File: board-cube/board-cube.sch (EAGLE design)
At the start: 95 parts, among them U1 TPS79933QDDCRQ1, U2 TPS79933QDDCRQ1, X1 SMA-142-0711-821/826, X10 SMA-142-0711-821/826, X2 SMA-142-0711-821/826, X3 SMA-142-0711-821/826, X4 SMA-142-0711-821/826, X5 SMA-142-0711-821/826, X6 SMA-142-0711-821/826, X7 SMA-142-0711-821/826, X8 SMA-142-0711-821/826, X9 SMA-142-0711-821/826

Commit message: more work
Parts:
- removed SV1, SV2: (no value), con-lstb:MA08-1
- added C4, C56: 100n, passives-7351:CAPACITOR0603-N
- added C57, C58: 1u, passives-7351:CAPACITOR0603-N
- added C59: 470n, passives-7351:CAPACITOR0603-N
- added C60: (no value), passives-7351:CAPACITOR0603-N
- added IC1: MSP430FR5739DA, Mine:MSP430FR5739DA
- added J1: TM4_SHIELD, cube-parts:TM4_SHIELD
- added JP10, JP9: (no value), SparkFun-Connectors:M03X22X3_SILK_MALE_PTH
- added JP5: FTDI_BASICPTH, SparkFun-Connectors:FTDI_BASICPTH
- added JP6: (no value), SparkFun-Connectors:M04PTH
- added LED1, LED2, LED3, LED4, LED5, LED6, LED7: (no value), dtb:LEDCHIP-LED0603
- added Q1: BSS84, transistor-small-signal:BSS84
- added R10, R11, R12, R13, R14, R8, R9: (no value), passives-7351:RESISTOR0603-N
- added R6, R7: 100k, passives-7351:RESISTOR0603-N
- added TP1, TP2, TP3: PTR1PAD1-20, testpad:PTR1PAD1-20
- R4: value 10k -> 100k
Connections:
- removed net N$43: SV2.2, U$4.CSN
- removed net N$44: SV2.1, U$4.NRESET
- removed net N$58: R4.P$1, U1.EN
- new net +3V3: C4.1, C56.1, C57.1, C58.1, IC1.AVCC, IC1.DVCC, J1.3V3, JP5.4
- new net A0_CLK: IC1.P1.5, JP9.3
- new net A0_CS: IC1.P1.4, JP9.1
- new net A0_SIMO: IC1.P2.0, JP9.5
- new net A1_RX: IC1.P2.6, J1.PB1, JP5.3
- new net A1_TX: IC1.P2.5, J1.PB0, JP5.2
- new net B0_CLK: IC1.P2.2, JP10.3
- new net B0_CS: IC1.P1.3, JP10.1
- new net B0_SIMO: IC1.P1.6, JP10.5
- new net INT_IN: IC1.P1.1, J1.PD7
- new net INT_OUT: IC1.P1.2, J1.PF4
- new net N$6: JP2.2, Q1.D
- new net RST: IC1.!RST, J1.RST
- new net RST_MAINBRD: IC1.P1.0, J1.PD6
- new net RX_CLK: J1.PA7, JP10.4, U$4.SCK
- new net RX_CS: J1.PA4, JP10.2, U$4.CSN
- new net RX_GPIO0: IC1.P3.5, J1.PC4, TP3.TP, U$4.GPIO0
- new net RX_GPIO2: IC1.P3.6, J1.PC5, U$4.GPIO2
- new net RX_GPIO3: IC1.P3.7, J1.PC6, U$4.GPIO3
- new net RX_MISO: IC1.P1.7, J1.PA6, U$4.MISO
- new net RX_MOSI: J1.PA5, JP10.6, U$4.MOSI
- new net RX_RST: IC1.P3.1, J1.PA2, R7.P$1, U$4.NRESET
- new net TX_CLK: J1.PB4, JP9.4, U$1.SCK
- new net TX_CS: J1.PE0, JP9.2, U$1.CSN
- new net TX_GPIO0: IC1.P3.2, J1.PF2, TP2.TP, U$1.GPIO0
- new net TX_GPIO2: IC1.P3.3, J1.PF3, U$1.GPIO2
- new net TX_GPIO3: IC1.P3.4, J1.PB3, U$1.GPIO3
- new net TX_MISO: IC1.P2.1, J1.PB6, U$1.MISO
- new net TX_MOSI: J1.PB7, JP9.6, U$1.MOSI
- new net TX_PA_EN: IC1.P2.4
- new net TX_RST: IC1.P3.0, J1.PA3, R6.P$1, U$1.NRESET
- new net VCORE: C59.2, IC1.VCORE
- net +5V: now also J1.VBUS, Q1.S, U1.EN; no longer JP2.2
- net GND: now also C4.2, C56.2, C57.2, C58.2, C59.1, C60.1, IC1.AVSS, IC1.DVSS, J1.GND, J1.GND1, JP5.6, LED1.C, LED2.C, LED3.C, LED4.C, R12.P$2, R13.P$2
- net N$10: now also LED1.A, R8.P$1; no longer SV1.8, U$1.GPIO0
- net N$11: now also LED2.A, R9.P$1; no longer SV1.7, U$1.GPIO2
- net N$12: now also LED3.A, R10.P$1; no longer SV1.6, U$1.GPIO3
- net N$13: now also TP1.TP, U$1.TRX_SW; no longer SV1.5, U$1.MOSI
- net N$14: now also LED4.A, R11.P$1; no longer SV1.4, U$1.MISO
- net N$15: now also IC1.PJ.3, R11.P$2; no longer SV1.3, U$1.SCK
- net N$16: now also IC1.TEST; no longer SV1.2, U$1.CSN
- net N$17: now also IC1.PJ.2, R10.P$2; no longer SV1.1, U$1.NRESET
- net N$37: now also IC1.PJ.1, R9.P$2; no longer SV2.8, U$4.GPIO0
- net N$38: now also IC1.PJ.0, R8.P$2; no longer SV2.7, U$4.GPIO2
- net N$39: now also C48.1, JP3.1, LED5.A, U1.OUT; no longer SV2.6, U$4.GPIO3
- net N$40: now also LED5.C, R12.P$1; no longer SV2.5, U$4.MOSI
- net N$41: now also LED6.C, R13.P$1; no longer SV2.4, U$4.MISO
- net N$42: now also LED7.A, R14.P$2; no longer SV2.3, U$4.SCK
- net N$51: now also R6.P$2
- net N$53: now also LED6.A
- net N$62: now also Q1.G, R4.P$1; no longer C48.1, JP3.1, U1.OUT
- net N$63: now also R7.P$2
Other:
- note added: "A0_SOMI"
- note added: "B0_SOMI"
- note added: "NEEDED? VALUE? >"
- note added: "clk"
- note added: "cs"
- note added: "miso"
- note added: "rx"
- note added: "set as open drain"
- note added: "simo"
- note added: "tx"
- moved on the sheet: C27, C28, C29, C30, C31, C32, C33, C34, C35, C36, C37, C38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

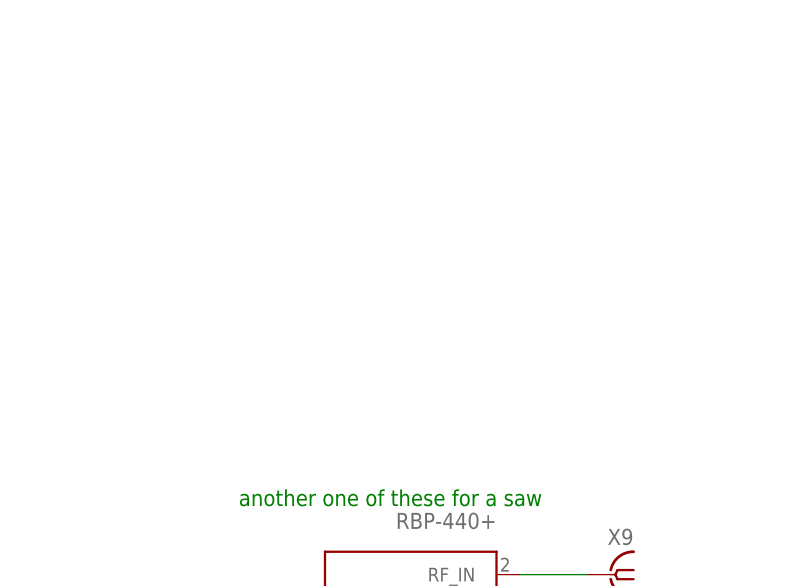
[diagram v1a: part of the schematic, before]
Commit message: Add 434MHz SAW and 2x SMA Connectors to sch,lbr.
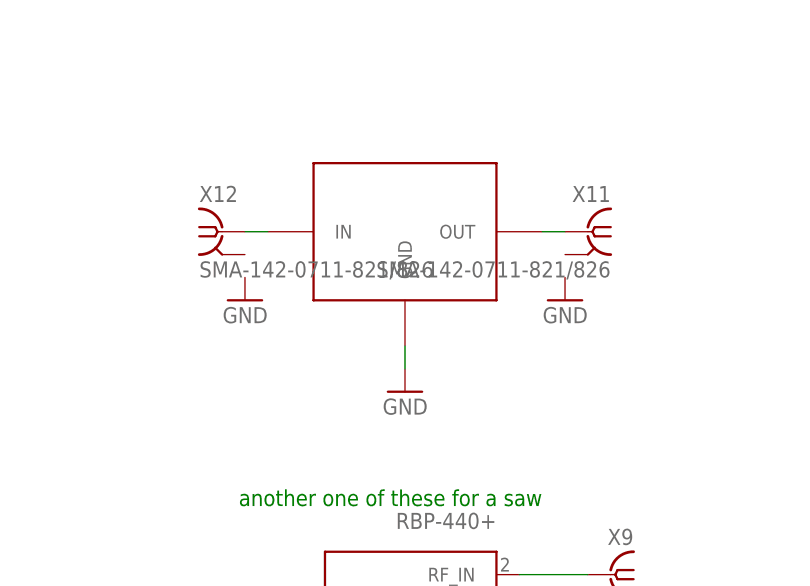
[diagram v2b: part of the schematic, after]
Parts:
- added U$7: GOLLEDGE_SAW_FILTER, Ava:GOLLEDGE_SAW_FILTER
- added X11, X12: SMA-142-0711-821/826, con-coax:SMA-142-0711-821/826
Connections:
- new net N$43: U$7.OUT, X11.1
- new net N$44: U$7.IN, X12.1
- net GND: now also U$7.GND
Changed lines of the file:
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@@
 <part name="LED7" library="dtb" deviceset="LED" device="CHIP-LED0603"/>
 <part name="R14" library="passives-7351" deviceset="RESISTOR" device="0603-N"/>
+<part name="U$7" library="Ava" deviceset="GOLLEDGE_SAW_FILTER" device=""/>
+<part name="X11" library="con-coax" deviceset="SMA-" device="142-0711-821/826"/>
+<part name="X12" library="con-coax" deviceset="SMA-" device="142-0711-821/826"/>
+<part name="GND78" library="supply1" deviceset="GND" device=""/>
+<part name="GND79" library="supply1" deviceset="GND" device=""/>
+<part name="GND80" library="supply1" deviceset="GND" device=""/>
 </parts>
 <sheets>
@@
 <instance part="LED7" gate="G$1" x="185.42" y="127"/>
 <instance part="R14" gate="G$1" x="185.42" y="134.62" rot="R270"/>
+<instance part="U$7" gate="G$1" x="261.62" y="-175.26"/>
+<instance part="X11" gate="G1" x="281.94" y="-175.26" rot="MR0"/>
+<instance part="X12" gate="G1" x="241.3" y="-175.26"/>
+<instance part="GND78" gate="1" x="243.84" y="-182.88" rot="MR0"/>
+<instance part="GND79" gate="1" x="279.4" y="-182.88" rot="MR0"/>
+<instance part="GND80" gate="1" x="261.62" y="-193.04" rot="MR0"/>
 </instances>
 <busses>
@@
 <pinref part="R13" gate="G$1" pin="P$2"/>
 <pinref part="GND77" gate="1" pin="GND"/>
+</segment>
+<segment>
+<pinref part="U$7" gate="G$1" pin="GND"/>
+<pinref part="GND80" gate="1" pin="GND"/>
+<wire x1="261.62" y1="-187.96" x2="261.62" y2="-190.5" width="0.1524" layer="91"/>
 </segment>
 </net>
@@
 </segment>
 </net>
+<net name="N$43" class="0">
+<segment>
+<pinref part="X11" gate="G1" pin="1"/>
+<pinref part="U$7" gate="G$1" pin="OUT"/>
+<wire x1="279.4" y1="-175.26" x2="276.86" y2="-175.26" width="0.1524" layer="91"/>
+</segment>
+</net>
+<net name="N$44" class="0">
+<segment>
+<pinref part="U$7" gate="G$1" pin="IN"/>
+<pinref part="X12" gate="G1" pin="1"/>
+<wire x1="246.38" y1="-175.26" x2="243.84" y2="-175.26" width="0.1524" layer="91"/>
+</segment>
+</net>

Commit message: added alternate PA
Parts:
- removed IC1: MSP430FR5739DA, Mine:MSP430FR5739DA
- removed J1: TM4_SHIELD, cube-parts:TM4_SHIELD
- removed JP6: (no value), SparkFun-Connectors:M04PTH
- added C61: 220p, passives-7351:CAPACITOR0603-N
- added C62: 33p, passives-7351:CAPACITOR0603-N
- added C63, C68: 100p, passives-7351:CAPACITOR0603-N
- added C64: 4.7u, passives-7351:CAPACITOR0603-N
- added C65: 1n, passives-7351:CAPACITOR0603-N
- added C66: 3.3p, passives-7351:CAPACITOR0603-N
- added C67, C69: 1u, passives-7351:CAPACITOR0603-N
- added C70: 15p, passives-7351:CAPACITOR0603-N
- added C71: 27p, passives-7351:CAPACITOR0603-N
- added IC3: MMZ09332BT1, CubeSat3:MMZ09332BT1
- added L10, L14, L15, L16: 33n, passives-7351:INDUCTOR0603-N
- added L17: 22n, passives-7351:INDUCTOR0603-N
- added R15: 2.2k, passives-7351:RESISTOR0603-N
- added R16: 1.8k, passives-7351:RESISTOR0603-N
- added X13, X14, X15: BU-SMA-V, con-coax:BU-SMA-V
- IC2: value PA -> LHA1+
- X1, X10, X11, X12, X2, X3, X4, X5, X6, X7, X8, X9: value SMA-142-0711-821/826 -> BU-SMA-V; device con-coax:SMA-142-0711-821/826 -> con-coax:BU-SMA-V
- renumbered U$2 to IC2
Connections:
- removed net INT_IN: IC1.P1.1, J1.PD7
- removed net INT_OUT: IC1.P1.2, J1.PF4
- removed net N$16: IC1.TEST
- removed net RST: IC1.!RST, J1.RST
- removed net RST_MAINBRD: IC1.P1.0, J1.PD6
- removed net TX_PA_EN: IC1.P2.4
- removed net VCORE: C59.2, IC1.VCORE
- new net N$58: C61.1, L10.P$1, L14.P$2
- new net N$64: C61.2, IC3.OUT, L15.P$1
- new net N$65: C62.1, L10.P$2, X15.1
- new net N$66: C63.1, IC3.PDET
- new net N$67: C64.1, C65.1, L15.P$2
- new net N$68: C66.1, IC3.VCC1, L16.P$1
- new net N$69: C67.1, L16.P$2
- new net N$70: IC3.VBA2, R16.P$2
- new net N$71: IC3.VBA1, R15.P$2
- new net N$72: C68.1, C69.1, IC3.VBIAS, R15.P$1, R16.P$1
- new net N$73: C70.1, L17.P$1, X14.1
- new net N$74: C71.1, IC3.IN, L17.P$2
- new net N$75: IC3.PDOWN
- new net N$76: C59.2
- net +3V3: no longer IC1.AVCC, IC1.DVCC, J1.3V3
- net +5V: no longer J1.VBUS
- net A0_CLK: no longer IC1.P1.5
- net A0_CS: no longer IC1.P1.4
- net A0_SIMO: no longer IC1.P2.0
- net A1_RX: no longer IC1.P2.6, J1.PB1
- net A1_TX: no longer IC1.P2.5, J1.PB0
- net B0_CLK: no longer IC1.P2.2
- net B0_CS: no longer IC1.P1.3
- net B0_SIMO: no longer IC1.P1.6
- net GND: now also C62.2, C63.2, C64.2, C65.2, C66.2, C67.2, C68.2, C69.2, C70.2, C71.2, IC3.GND, L14.P$1, X14.2, X15.2; no longer IC1.AVSS, IC1.DVSS, J1.GND, J1.GND1
- net N$15: no longer IC1.PJ.3
- net N$17: no longer IC1.PJ.2
- net N$27: now also X4.1; no longer X3.1
- net N$28: now also X3.1; no longer X4.1
- net N$37: no longer IC1.PJ.1
- net N$38: no longer IC1.PJ.0
- net RX_CLK: no longer J1.PA7
- net RX_CS: no longer J1.PA4
- net RX_GPIO0: no longer IC1.P3.5, J1.PC4
- net RX_GPIO2: no longer IC1.P3.6, J1.PC5
- net RX_GPIO3: no longer IC1.P3.7, J1.PC6
- net RX_MISO: no longer IC1.P1.7, J1.PA6
- net RX_MOSI: no longer J1.PA5
- net RX_RST: no longer IC1.P3.1, J1.PA2
- net TX_CLK: no longer J1.PB4
- net TX_CS: no longer J1.PE0
- net TX_GPIO0: no longer IC1.P3.2, J1.PF2
- net TX_GPIO2: no longer IC1.P3.3, J1.PF3
- net TX_GPIO3: no longer IC1.P3.4, J1.PB3
- net TX_MISO: no longer IC1.P2.1, J1.PB6
- net TX_MOSI: no longer J1.PB7
- net TX_RST: no longer IC1.P3.0, J1.PA3
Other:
- note added: "mcl lha1+"
- note added: "package ok"

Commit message: adding supervising processor
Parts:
- added C72: (no value), passives-7351:CAPACITOR0805-N
- added C73, C74: 1u, passives-7351:CAPACITOR0603-N
- added C75: 100n, passives-7351:CAPACITOR0603-N
- added IC1: MSP430FR2110PW, CubeSat3:MSP430FR2110PW
- added JP6, JP7: M02PTH, SparkFun-Connectors:M02PTH
- added L18, L19, L20: 0R, passives-7351:INDUCTOR0603-N
- added LED8, LED9: (no value), dtb:LEDCHIP-LED0603
- added R17, R19: (no value), passives-7351:RESISTOR0603-N
- added R18: 4k7, passives-7351:RESISTOR0603-N
- added X16, X17: BU-SMA-V, con-coax:BU-SMA-V
- C4, C56: value 100n -> dnp
- C57, C58: value 1u -> dnp
- C59: value 470n -> (none); device passives-7351:CAPACITOR0603-N -> passives-7351:CAPACITOR0805-N
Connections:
- new net N$16: C4.2, L18.P$1, X16.1
- new net N$77: C57.2, L19.P$2, L20.P$1
- new net N$78: C58.2, L20.P$2, X17.1
- new net N$79: C25.2, C54.1, C55.1, JP2.1, L5.P$2, LED8.A
- new net N$80: C73.1, C74.1, C75.1, IC1.VCC
- net +3V3: no longer C4.1, C56.1, C57.1, C58.1
- net GND: now also C4.1, C56.1, C57.1, C58.1, C59.2, C72.2, C73.2, C74.2, C75.2, IC1.VSS, R14.P$2, R17.P$2, R18.P$1, R19.P$2, X16.2, X17.2; no longer C4.2, C56.2, C57.2, C58.2, C59.1
- net N$24: now also C59.1, C64.1, C65.1, C67.1, C68.1, C69.1, C72.1, IC3.VBIAS, JP6.1, L15.P$2, L16.P$2, R15.P$1, R16.P$1; no longer C25.2, C54.1, C55.1, JP2.1, L5.P$2
- net N$42: now also LED7.C, R14.P$1; no longer LED7.A, R14.P$2
- net N$52: now also LED7.A
- net N$6: now also JP6.2
- net N$62: now also JP7.1
- net N$67: now also LED8.C, R17.P$1; no longer C64.1, C65.1, L15.P$2
- net N$69: now also JP7.2, R18.P$2; no longer C67.1, L16.P$2
- net N$72: now also LED9.C, R19.P$1; no longer C68.1, C69.1, IC3.VBIAS, R15.P$1, R16.P$1
- net N$76: now also C56.2, L18.P$2, L19.P$1; no longer C59.2
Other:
- note added: "add other lna"
- note removed: "rx"
- note removed: "tx"
- moved on the sheet: C4, C56, C57, C58, C59, LED7, R14
